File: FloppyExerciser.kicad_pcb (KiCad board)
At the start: 2 copper layers, 100 x 100 mm, 112 parts, among them J1 STEPPER, J10 IBM 31SD, J11 PS/2, J12 APPLE II, J2 WRITE, J3 ISP, J4 V, J6 IBM, J7 HP 34-PIN, J8 HP 26-PIN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

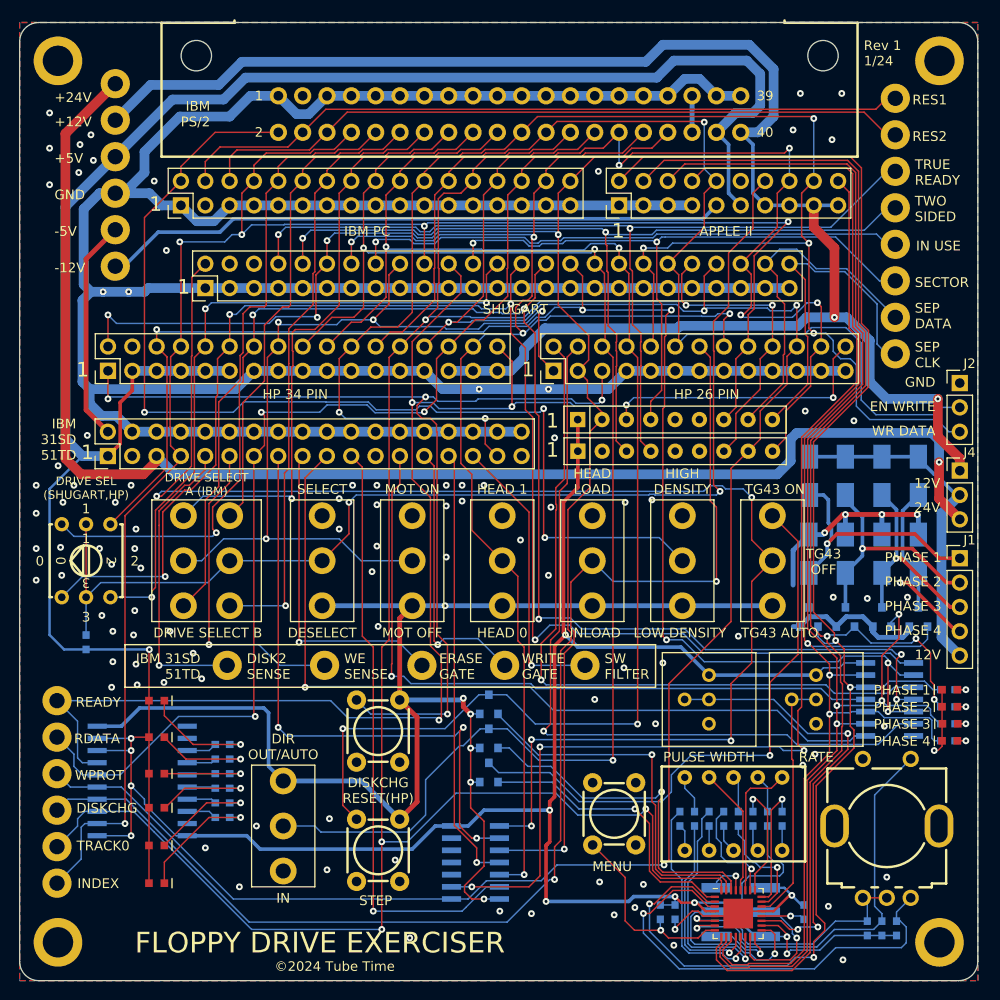
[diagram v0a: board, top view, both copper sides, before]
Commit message: Rev2 fab with minor fixes for HP 26 pin
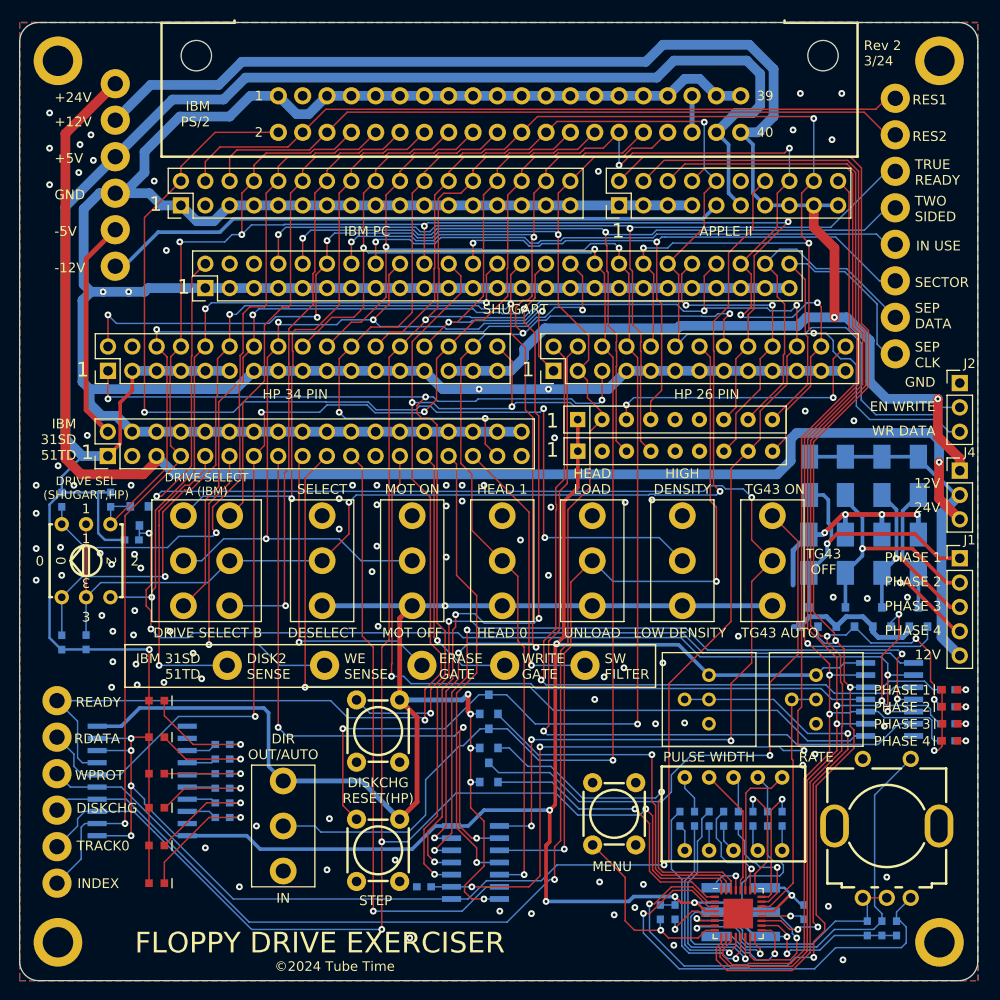
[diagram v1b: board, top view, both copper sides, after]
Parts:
- added Q8: ~, Active:SOT95P230X117-3, B.Cu at (112.5, 101.5)
- added R22: 3.3K, Passive:RESC1608X55, B.Cu at (142.2, 140.2)
- added R23: 10K, Passive:RESC1608X55, B.Cu at (104.4, 114.7)
- added R26: 10K, Passive:RESC1608X55, B.Cu at (104.4, 99.8)
- added R27: 10K, Passive:RESC1608X55, B.Cu at (109.5, 99.8)
- added R28: 10K, Passive:RESC1608X55, B.Cu at (111.7, 104.0)
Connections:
- U3 pad 1: /DSEL_1 -> Net-(U3-Pad1)
- U3 pad 2: /DSEL_3 -> Net-(Q8-D)
- U3 pad 4: /DSEL_2 -> Net-(U3-Pad4)
- U3 pad 5: /DSEL_3 -> Net-(Q8-D)
- U4 pad 10: unconnected-(U4-Pad10) -> Net-(U3-Pad4)
- U4 pad 11: GND -> /DSEL_2
- U4 pad 12: unconnected-(U4-Pad12) -> Net-(U3-Pad1)
- U4 pad 13: GND -> /DSEL_1
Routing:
- net Net-(Q8-D): track 0.00 -> 102.2 mm, vias 0 -> 4
- net Net-(U3-Pad4): track 0.00 -> 85.1 mm, vias 0 -> 4
- net /DSEL_3: track 154.3 -> 78.2 mm, vias 6 -> 2
- net Net-(U3-Pad1): track 0.00 -> 74.2 mm, vias 0 -> 2
- net +5V: track 408.8 -> 421.8 mm
- net /DSEL_1: track 155.0 -> 148.8 mm, vias 4 -> 6
- net /DSEL_2: track 155.4 -> 150.6 mm
- net Net-(J12-Pin_20): track 113.9 -> 116.1 mm
- net Net-(J10-Pin_29): track 46.0 -> 47.8 mm
- net /DISKCH_RST: track 103.7 -> 102.3 mm
- net GND: track 576.0 -> 576.9 mm, vias 110 -> 109
- net /READY: track 160.7 -> 159.9 mm
- net /WRITE_GATE: track 28.7 -> 27.9 mm
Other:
- board text added: "Rev 2 3/24"
- board text removed: "Rev 1 1/24"
